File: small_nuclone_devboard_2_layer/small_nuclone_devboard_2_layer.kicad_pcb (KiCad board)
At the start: 2 copper layers, 50 x 50 mm, 42 parts, among them J1 JTAG_2X05, J2 TYPE-C-31-M-12, J3 nuclone_small_left, J4 nuclone_small_right, SW1 RESET, SW2 Bootloader, U1 MCP1702-MB, U2 TPESD0504C6

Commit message: fixed changed openhardware logo footprint
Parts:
- N1: footprint Symbols:OSHW-Symbol_6.7x6mm_SilkScreen -> Symbol:OSHW-Symbol_6.7x6mm_SilkScreen
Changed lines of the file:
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@@
     )
   )
-  (footprint "Symbols:OSHW-Symbol_6.7x6mm_SilkScreen" (layer "B.Cu")
+  (footprint "Symbol:OSHW-Symbol_6.7x6mm_SilkScreen" (layer "B.Cu")
     (at 84.85 103.65 180)
     (descr "Open Source Hardware Symbol")

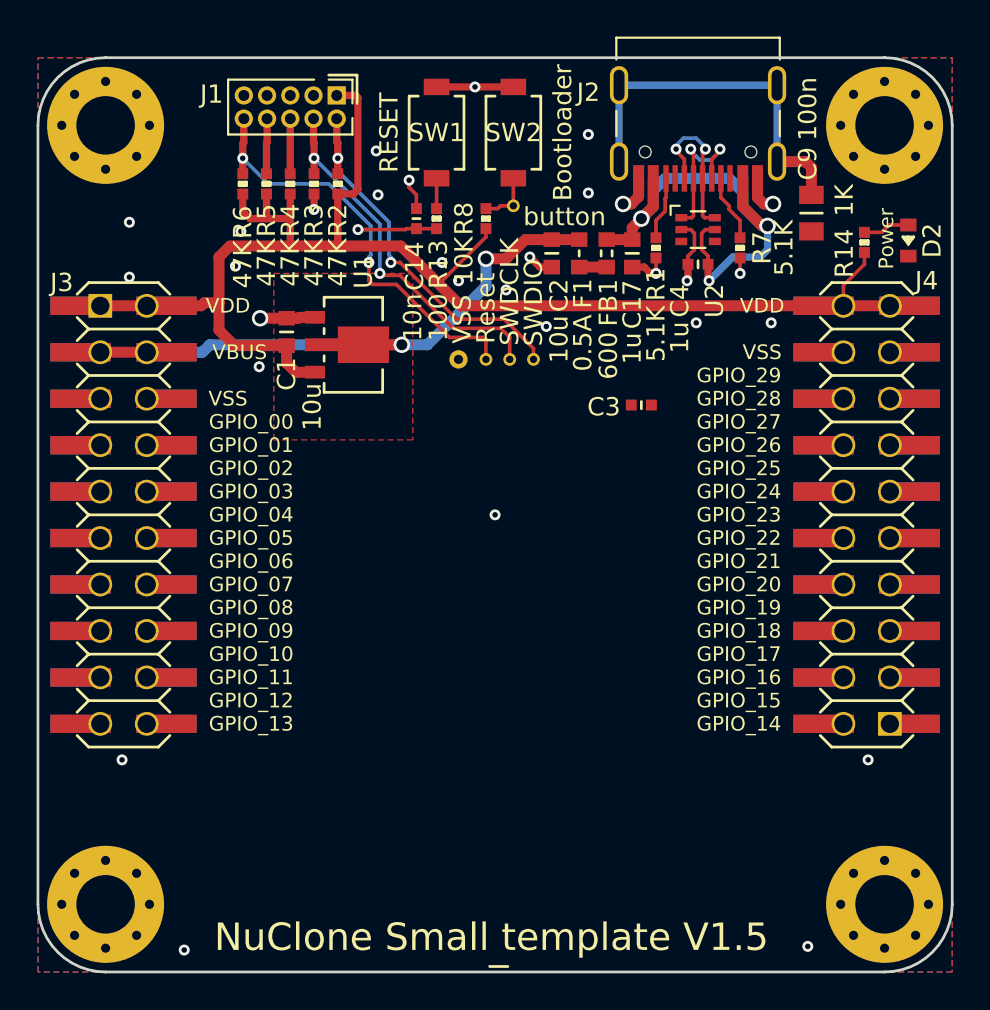
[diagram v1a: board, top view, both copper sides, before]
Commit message: switched testpoints to test connector, changed via sizes
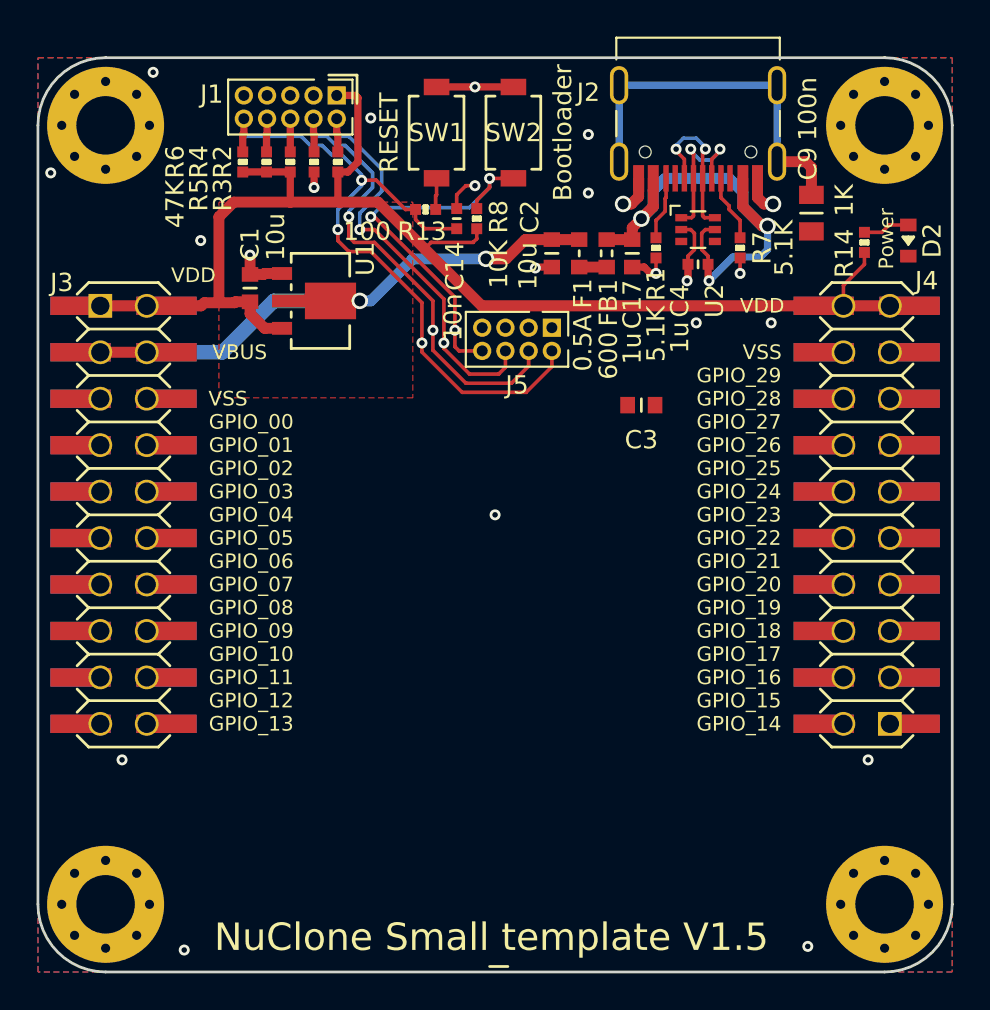
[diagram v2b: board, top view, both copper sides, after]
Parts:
- removed TP1: SWDIO, SquantorTestPoints:TestPoint_hole_H04R07
- removed TP2: SWDCLK, SquantorTestPoints:TestPoint_hole_H04R07
- removed TP3: VSS, SquantorTestPoints:TestPoint_hole_H05R10
- removed TP4: button, SquantorTestPoints:TestPoint_hole_H04R07
- removed TP5: Reset, SquantorTestPoints:TestPoint_hole_H04R07
- added J5: Conn_02x06_Odd_Even, SquantorConnectors:Header-0127-2X04-H006, F.Cu at (86.2, 76.4)
- C3: value 1u -> 10u; footprint SquantorRcl:C_0402 -> SquantorRcl:C_0603
- moved C1 3.12 mm to (71.6, 73.6)
- moved U1 3.00 mm to (75.1, 74.3)
- moved C14 2.20 mm to (82.9, 69.8)
- moved R2 1.20 mm to (76.4, 66.7)
- moved R3 1.20 mm to (75.1, 66.7)
- moved R4 1.20 mm to (73.8, 66.7)
- moved R5 1.20 mm to (72.5, 66.7)
- moved R6 1.20 mm to (71.2, 66.7)
- moved R13 0.78 mm to (81.2, 69.3), turned to 0 degrees
- moved R8 0.50 mm to (84.0, 69.8)
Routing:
- net /Bootloader: track 3.06 -> 21.6 mm, vias 0 -> 3
- net /RESET: track 28.5 -> 39.0 mm
- net /VDD: track 83.5 -> 76.3 mm
- net /TCK: track 20.6 -> 26.8 mm
- net /TMS: track 20.3 -> 23.6 mm
- net /VBUS: track 33.1 -> 31.6 mm
- net /TDO: track 3.02 -> 1.82 mm
- net /TDI: track 3.03 -> 1.83 mm
- net /VSS: track 22.0 -> 21.5 mm, vias 30 -> 23
